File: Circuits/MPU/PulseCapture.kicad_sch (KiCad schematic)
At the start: 24 parts, among them U32 LT1715, U33 ADA4805-2ARMZ, U34 AD7984BRMZ

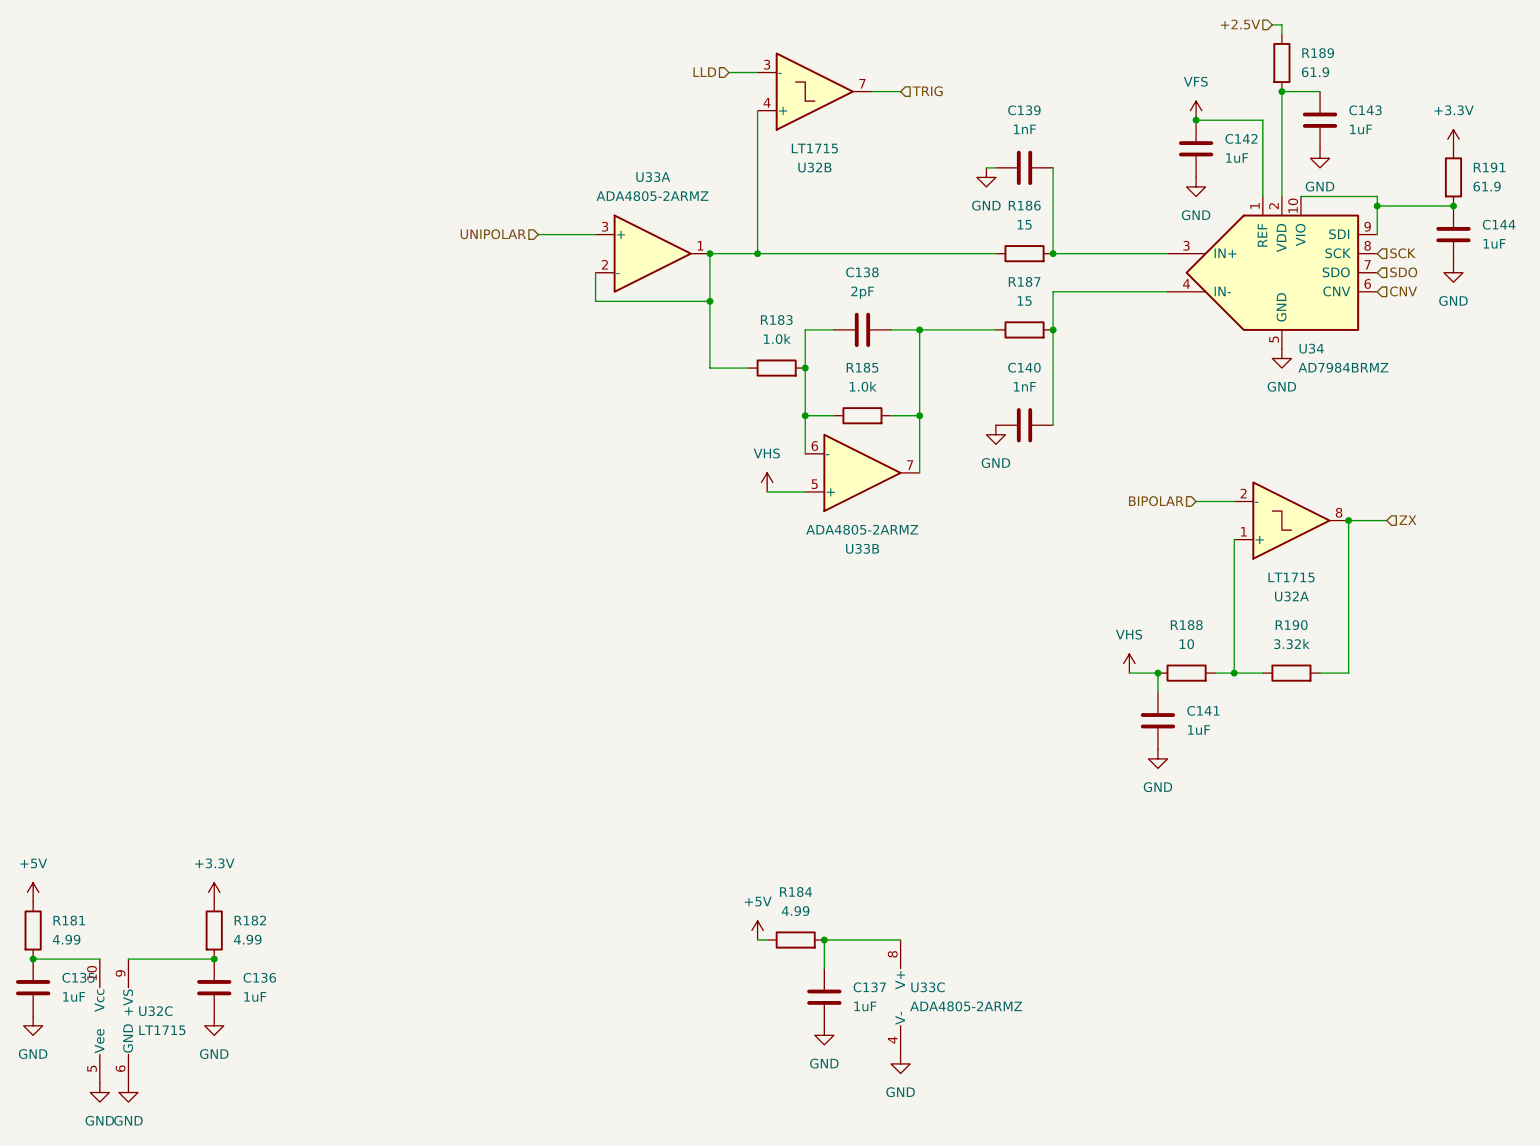
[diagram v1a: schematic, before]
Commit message: Files changed due to KiCAD update
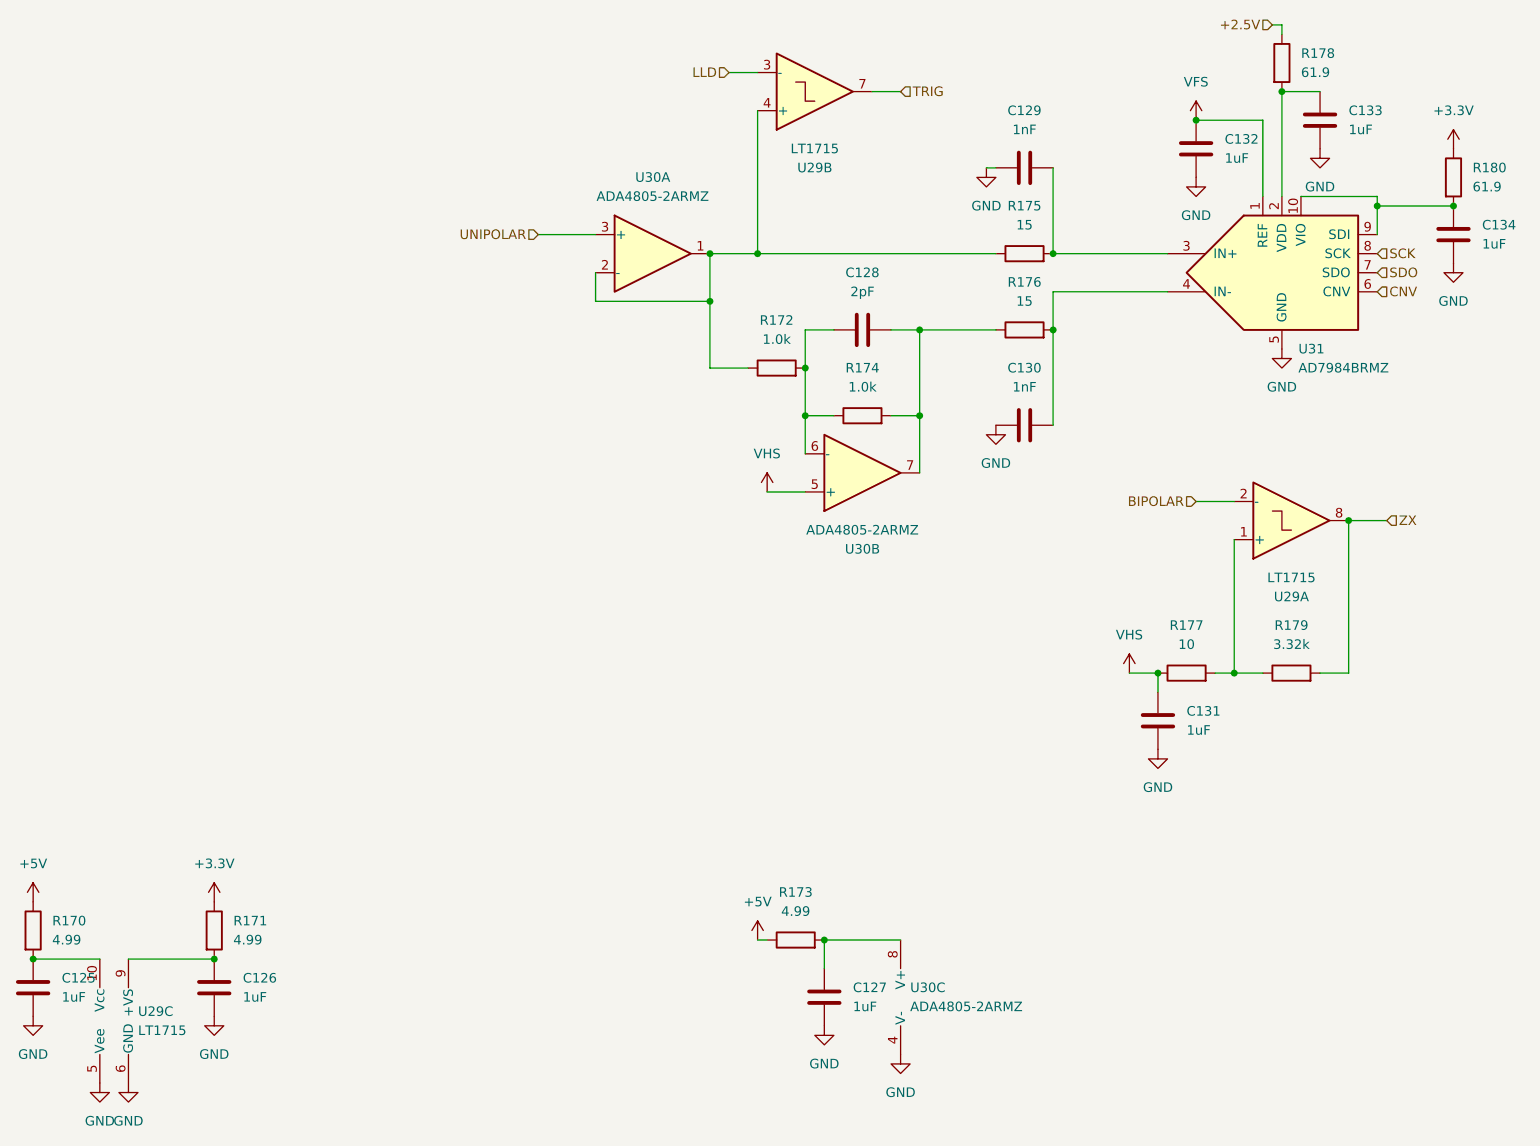
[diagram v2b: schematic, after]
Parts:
- renumbered C135 to C125, C136 to C126, C137 to C127, C138 to C128, C139 to C129, C140 to C130, C141 to C131, C142 to C132, C143 to C133, C144 to C134, R181 to R170, R182 to R171, R183 to R172, R184 to R173, R185 to R174, R186 to R175, R187 to R176, R188 to R177, R189 to R178, R190 to R179, R191 to R180, U32 to U29, U33 to U30, U34 to U31
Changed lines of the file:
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@@
 (kicad_sch
-	(version 20231120)
+	(version 20250114)
 	(generator "eeschema")
-	(generator_version "8.0")
+	(generator_version "9.0")
 	(paper "USLetter")
 	(title_block
@@
 		(shape input)
 		(at 138.43 63.5 0)
-		(fields_autoplaced yes)
 		(effects
 			(font
@@
 		(shape input)
 		(at 201.93 90.17 0)
-		(fields_autoplaced yes)
 		(effects
 			(font
@@
 		(shape input)
 		(at 187.96 54.61 180)
-		(fields_autoplaced yes)
 		(effects
 			(font
@@
 		(shape input)
 		(at 90.17 82.55 180)
-		(fields_autoplaced yes)
 		(effects
 			(font
@@
 		(shape input)
 		(at 177.8 118.11 180)
-		(fields_autoplaced yes)
 		(effects
 			(font
@@
 		(shape input)
 		(at 201.93 87.63 0)
-		(fields_autoplaced yes)
 		(effects
 			(font
@@
 		(shape input)
 		(at 201.93 85.09 0)
-		(fields_autoplaced yes)
 		(effects
 			(font
@@
 		(shape input)
 		(at 203.2 120.65 0)
-		(fields_autoplaced yes)
 		(effects
 			(font
@@
 		(shape input)
 		(at 115.57 60.96 180)
-		(fields_autoplaced yes)
 		(effects
 			(font
@@
 		(dnp no)
 		(fields_autoplaced yes)
-		(property "Reference" "#PWR0270"
+		(property "Reference" "#PWR0250"
 			(at 31.75 201.93 0)
 			(effects
@@
 		(dnp no)
 		(fields_autoplaced yes)
-		(property "Reference" "C143"
+		(property "Reference" "C133"
 			(at 198.12 66.04 0)
 			(effects
@@
 		(dnp no)
 		(fields_autoplaced yes)
-		(property "Reference" "C140"
+		(property "Reference" "C130"
 			(at 154.94 100.33 90)
 			(effects
@@
 		(on_board yes)
 		(dnp no)
-		(property "Reference" "U33"
+		(property "Reference" "U30"
 			(at 133.35 124.46 0)
 			(effects
@@
 		(dnp no)
 		(fields_autoplaced yes)
-		(property "Reference" "C137"
+		(property "Reference" "C127"
 			(at 132.08 182.88 0)
 			(effects
@@
 		(dnp no)
 		(fields_autoplaced yes)
-		(property "Reference" "C144"
+		(property "Reference" "C134"
 			(at 215.9 81.28 0)
 			(effects
@@
 		(dnp no)
 		(fields_autoplaced yes)
-		(property "Reference" "R187"
+		(property "Reference" "R176"
 			(at 154.94 88.9 90)
 			(effects
@@
 		(dnp no)
 		(fields_autoplaced yes)
-		(property "Reference" "#PWR0281"
+		(property "Reference" "#PWR0261"
 			(at 172.72 157.48 0)
 			(effects
@@
 		(dnp no)
 		(fields_autoplaced yes)
-		(property "Reference" "#PWR0269"
+		(property "Reference" "#PWR0249"
 			(at 22.86 193.04 0)
 			(effects
@@
 		(dnp no)
 		(fields_autoplaced yes)
-		(property "Reference" "U33"
+		(property "Reference" "U30"
 			(at 139.7 182.88 0)
 			(effects
@@
 		(dnp no)
 		(fields_autoplaced yes)
-		(property "Reference" "C138"
+		(property "Reference" "C128"
 			(at 133.35 87.63 90)
 			(effects
@@
 		(dnp no)
 		(fields_autoplaced yes)
-		(property "Reference" "#PWR0272"
+		(property "Reference" "#PWR0252"
 			(at 46.99 175.26 0)
 			(effects
@@
 		(dnp no)
 		(fields_autoplaced yes)
-		(property "Reference" "#PWR0287"
+		(property "Reference" "#PWR0267"
 			(at 212.09 92.71 0)
 			(effects
@@
 		(dnp no)
 		(fields_autoplaced yes)
-		(property "Reference" "U33"
+		(property "Reference" "U30"
 			(at 105.41 74.93 0)
 			(effects
@@
 		(dnp no)
 		(fields_autoplaced yes)
-		(property "Reference" "R184"
+		(property "Reference" "R173"
 			(at 124.46 170.18 90)
 			(effects
@@
 		(dnp no)
 		(fields_autoplaced yes)
-		(property "Reference" "#PWR0268"
+		(property "Reference" "#PWR0248"
 			(at 22.86 175.26 0)
 			(effects
@@
 		(dnp no)
 		(fields_autoplaced yes)
-		(property "Reference" "R186"
+		(property "Reference" "R175"
 			(at 154.94 78.74 90)
 			(effects
@@
 		(dnp no)
 		(fields_autoplaced yes)
-		(property "Reference" "#PWR0283"
+		(property "Reference" "#PWR0263"
 			(at 177.8 81.28 0)
 			(effects
@@
 		(dnp no)
 		(fields_autoplaced yes)
-		(property "Reference" "#PWR0279"
+		(property "Reference" "#PWR0259"
 			(at 151.13 114.3 0)
 			(effects
@@
 		(dnp no)
 		(fields_autoplaced yes)
-		(property "Reference" "#PWR0286"
+		(property "Reference" "#PWR0266"
 			(at 212.09 74.93 0)
 			(effects
@@
 		(dnp no)
 		(fields_autoplaced yes)
-		(property "Reference" "#PWR0278"
+		(property "Reference" "#PWR0258"
 			(at 149.86 80.01 0)
 			(effects
@@
 		(dnp no)
 		(fields_autoplaced yes)
-		(property "Reference" "R189"
+		(property "Reference" "R178"
 			(at 191.77 58.42 0)
 			(effects
@@
 		(dnp no)
 		(fields_autoplaced yes)
-		(property "Reference" "R188"
+		(property "Reference" "R177"
 			(at 176.53 134.62 90)
 			(effects
@@
 		(dnp no)
 		(fields_autoplaced yes)
-		(property "Reference" "#PWR0275"
+		(property "Reference" "#PWR0255"
 			(at 120.65 120.65 0)
 			(effects
@@
 		(dnp no)
 		(fields_autoplaced yes)
-		(property "Reference" "C136"
+		(property "Reference" "C126"
 			(at 50.8 181.61 0)
 			(effects
@@
 		(dnp no)
 		(fields_autoplaced yes)
-		(property "Reference" "C135"
+		(property "Reference" "C125"
 			(at 26.67 181.61 0)
 			(effects
@@
 		(on_board yes)
 		(dnp no)
-		(property "Reference" "U32"
+		(property "Reference" "U29"
 			(at 190.5 130.81 0)
 			(effects
@@
 		(dnp no)
 		(fields_autoplaced yes)
-		(property "Reference" "#PWR0276"
+		(property "Reference" "#PWR0256"
 			(at 128.27 194.31 0)
 			(effects
@@
 		(dnp no)
 		(fields_autoplaced yes)
-		(property "Reference" "C142"
+		(property "Reference" "C132"
 			(at 181.61 69.85 0)
 			(effects
@@
 		(dnp no)
 		(fields_autoplaced yes)
-		(property "Reference" "#PWR0285"
+		(property "Reference" "#PWR0265"
 			(at 194.31 77.47 0)
 			(effects
@@
 		(dnp no)
 		(fields_autoplaced yes)
-		(property "Reference" "C139"
+		(property "Reference" "C129"
 			(at 154.94 66.04 90)
 			(effects
@@
 		(dnp no)
 		(fields_autoplaced yes)
-		(property "Reference" "C141"
+		(property "Reference" "C131"
 			(at 176.53 146.05 0)
 			(effects
@@
 		(dnp no)
 		(fields_autoplaced yes)
-		(property "Reference" "R191"
+		(property "Reference" "R180"
 			(at 214.63 73.66 0)
 			(effects
@@
 		(dnp no)
 		(fields_autoplaced yes)
-		(property "Reference" "#PWR0282"
+		(property "Reference" "#PWR0262"
 			(at 177.8 71.12 0)
 			(effects
@@
 		(dnp no)
 		(fields_autoplaced yes)
-		(property "Reference" "R181"
+		(property "Reference" "R170"
 			(at 25.4 173.99 0)
 			(effects
@@
 		(dnp no)
 		(fields_autoplaced yes)
-		(property "Reference" "R183"
+		(property "Reference" "R172"
 			(at 121.92 93.98 90)
 			(effects
@@
 		(dnp no)
 		(fields_autoplaced yes)
-		(property "Reference" "R182"
+		(property "Reference" "R171"
 			(at 49.53 173.99 0)
 			(effects
@@
 		(dnp no)
 		(fields_autoplaced yes)
-		(property "Reference" "U34"
+		(property "Reference" "U31"
 			(at 191.4241 97.79 0)
 			(effects
@@
 		(dnp no)
 		(fields_autoplaced yes)
-		(property "Reference" "#PWR0277"
+		(property "Reference" "#PWR0257"
 			(at 138.43 198.12 0)
 			(effects
@@
 		(dnp no)
 		(fields_autoplaced yes)
-		(property "Reference" "R185"
+		(property "Reference" "R174"
 			(at 133.35 100.33 90)
 			(effects
@@
 		(dnp no)
 		(fields_autoplaced yes)
-		(property "Reference" "#PWR0273"
+		(property "Reference" "#PWR0253"
 			(at 46.99 193.04 0)
 			(effects
@@
 		(dnp no)
 		(fields_autoplaced yes)
-		(property "Reference" "#PWR0284"
+		(property "Reference" "#PWR0264"
 			(at 189.23 104.14 0)
 			(effects
@@
 		(dnp no)
 		(fields_autoplaced yes)
-		(property "Reference" "#PWR0280"
+		(property "Reference" "#PWR0260"
 			(at 168.91 144.78 0)
 			(effects
@@
 		(dnp no)
 		(fields_autoplaced yes)
-		(property "Reference" "#PWR0274"
+		(property "Reference" "#PWR0254"
 			(at 119.38 180.34 0)
 			(effects
@@
 		(on_board yes)
 		(dnp no)
-		(property "Reference" "U32"
+		(property "Reference" "U29"
 			(at 127 73.66 0)
 			(effects
@@
 		(dnp no)
 		(fields_autoplaced yes)
-		(property "Reference" "U32"
+		(property "Reference" "U29"
 			(at 36.83 186.055 0)
 			(effects
@@
 		(dnp no)
 		(fields_autoplaced yes)
-		(property "Reference" "R190"
+		(property "Reference" "R179"
 			(at 190.5 134.62 90)
 			(effects
@@
 		(dnp no)
 		(fields_autoplaced yes)
-		(property "Reference" "#PWR0271"
+		(property "Reference" "#PWR0251"
 			(at 35.56 201.93 0)
 			(effects

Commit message: S/H for fast channel. Higher HV.
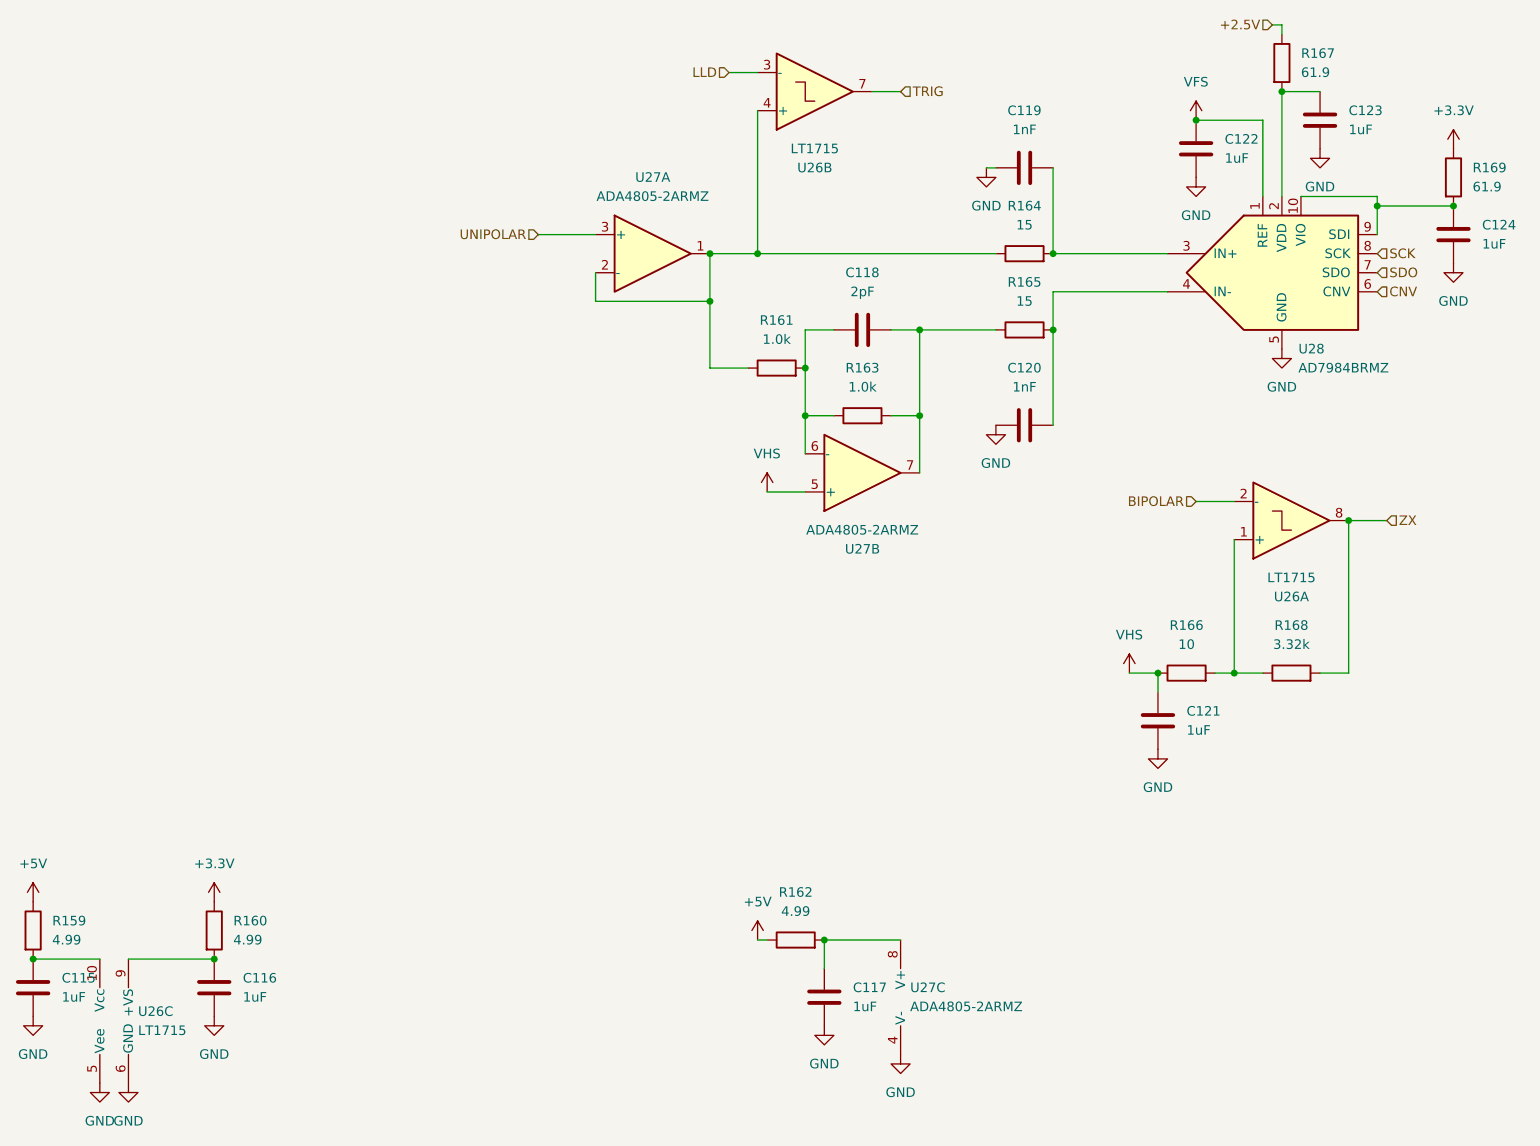
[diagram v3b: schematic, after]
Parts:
- renumbered C125 to C115, C126 to C116, C127 to C117, C128 to C118, C129 to C119, C130 to C120, C131 to C121, C132 to C122, C133 to C123, C134 to C124, R170 to R159, R171 to R160, R172 to R161, R173 to R162, R174 to R163, R175 to R164, R176 to R165, R177 to R166, R178 to R167, R179 to R168, R180 to R169, U29 to U26, U30 to U27, U31 to U28
